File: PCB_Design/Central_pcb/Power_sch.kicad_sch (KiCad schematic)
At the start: 1 part

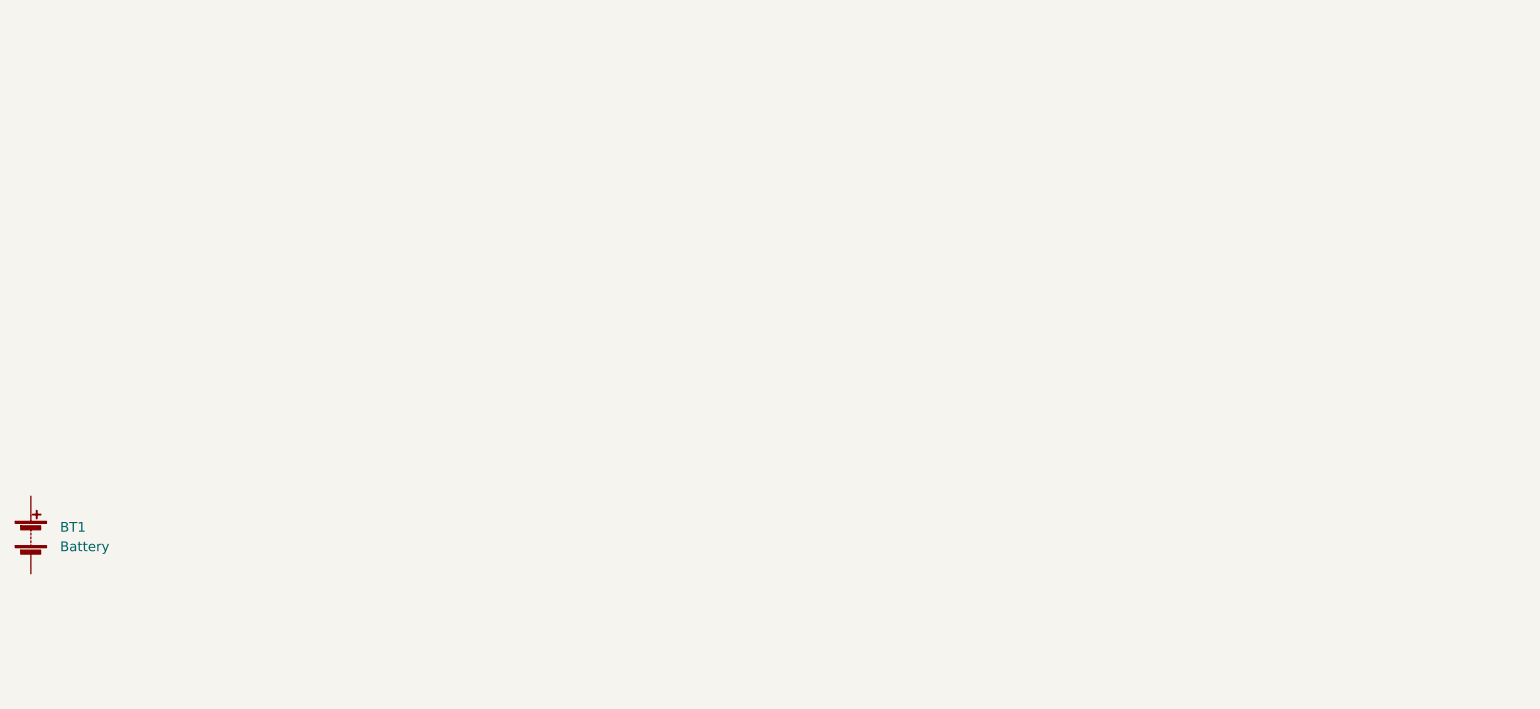
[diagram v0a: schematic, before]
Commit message: Power part added
Power part is finished with power footprints
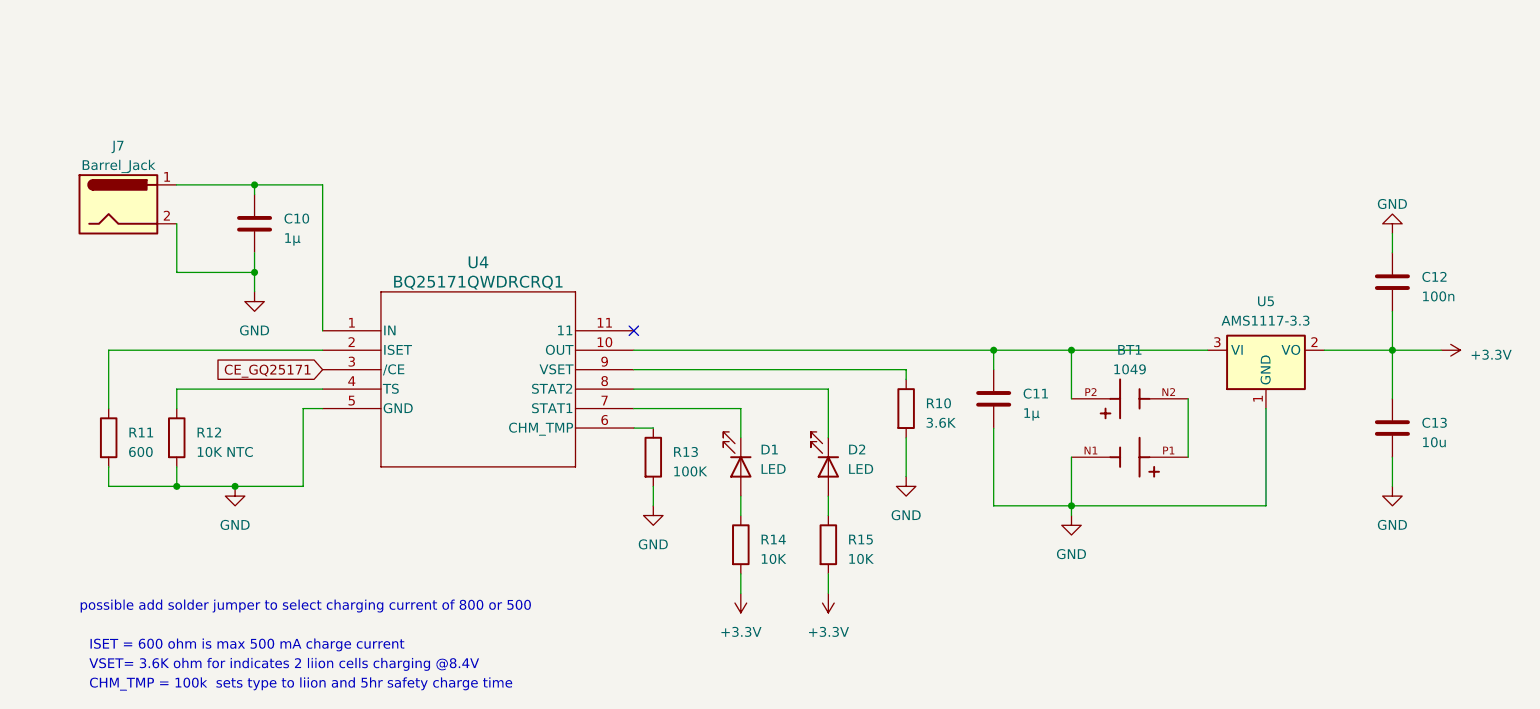
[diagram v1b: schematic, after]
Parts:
- removed BT1: Battery, symbol Device:Battery
- added BT1: 1049, Central:BAT_1049, symbol 1049P:1049
- added C10, C11: 1µ, Capacitor_SMD:C_0805_2012Metric_Pad1.18x1.45mm_HandSolder, symbol Device:C
- added C12: 100n, Capacitor_SMD:C_0805_2012Metric_Pad1.18x1.45mm_HandSolder, symbol Device:C
- added C13: 10u, Capacitor_SMD:C_0805_2012Metric_Pad1.18x1.45mm_HandSolder, symbol Device:C
- added D1, D2: LED, LED_SMD:LED_0805_2012Metric_Pad1.15x1.40mm_HandSolder, symbol Device:LED
- added J7: Barrel_Jack, Connector_BarrelJack:BarrelJack_GCT_DCJ200-10-A_Horizontal, symbol Connector:Barrel_Jack
- added R10: 3.6K, Resistor_SMD:R_0805_2012Metric_Pad1.20x1.40mm_HandSolder, symbol Device:R
- added R11: 600, Resistor_SMD:R_0805_2012Metric_Pad1.20x1.40mm_HandSolder, symbol Device:R
- added R12: 10K NTC, symbol Device:R
- added R13: 100K, Resistor_SMD:R_0805_2012Metric_Pad1.20x1.40mm_HandSolder, symbol Device:R
- added R14, R15: 10K, Resistor_SMD:R_0805_2012Metric_Pad1.20x1.40mm_HandSolder, symbol Device:R
- added U4: BQ25171QWDRCRQ1, Central:VSON10_BQ25171_3X3_TEX, symbol BQ25171:BQ25171QWDRCRQ1
- added U5: AMS1117-3.3, Package_TO_SOT_SMD:SOT-223-3_TabPin2, symbol Regulator_Linear:AMS1117-3.3
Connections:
- new net: D2.1 (K), U4.8 (STAT2)
- new net: D2.2 (A), R15.1
- new net: C10.1, J7.1, U4.1 (IN)
- new net: R11.1, U4.2 (ISET)
- new net: BT1.N2, BT1.P1
- new net: BT1.P2, C11.1, U4.10 (OUT), U5.3 (VI)
- new net: R13.1, U4.6 (CHM_TMP)
- new net: D1.1 (K), U4.7 (STAT1)
- new net: D1.2 (A), R14.1
- new net: R12.1, U4.4 (TS)
- new net: R10.1, U4.9 (VSET)
- new net +3.3V: C12.2, C13.1, R14.2, R15.2, U5.2 (VO)
- new net CE_GQ25171: U4.3 (/CE)
- new net GND: BT1.N1, C10.2, C11.2, C12.1, C13.2, J7.2, R10.2, R11.2, R12.2, R13.2, U4.5 (GND), U5.1 (GND)
- no-connect marks 0 -> 1
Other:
- note added: "CHM_TMP = 100k sets type to liion and 5hr safety charge time"
- note added: "ISET = 600 ohm is max 500 mA charge current"
- note added: "VSET= 3.6K ohm for indicates 2 liion cells charging @8.4V"
- note added: "possible add solder jumper to select charging current of 800 or 500"

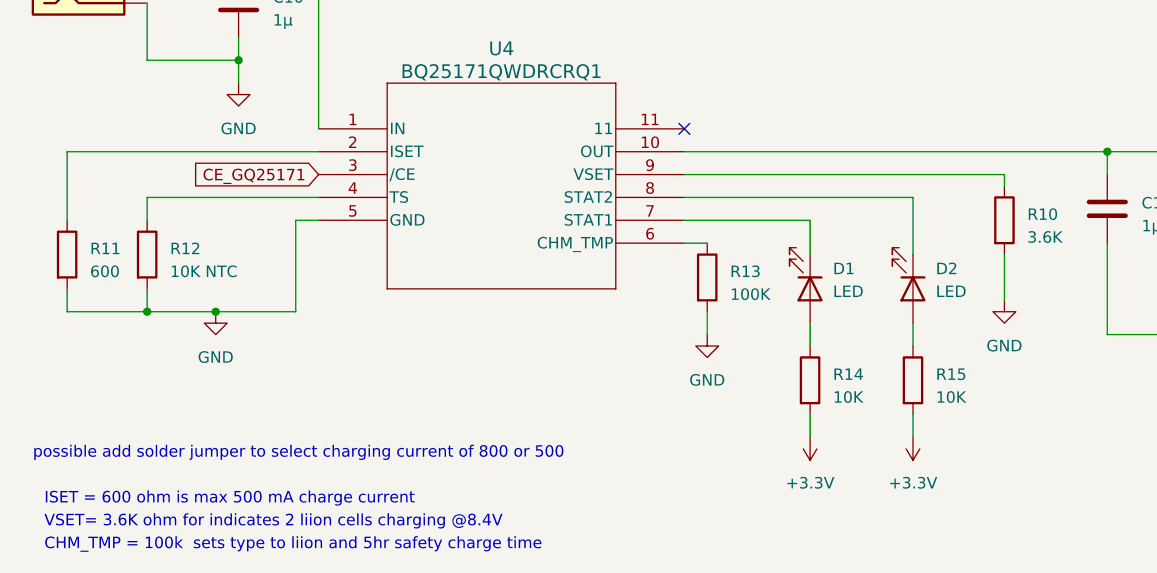
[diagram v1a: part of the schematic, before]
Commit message: Scematic update
update scematic and added some footrpints
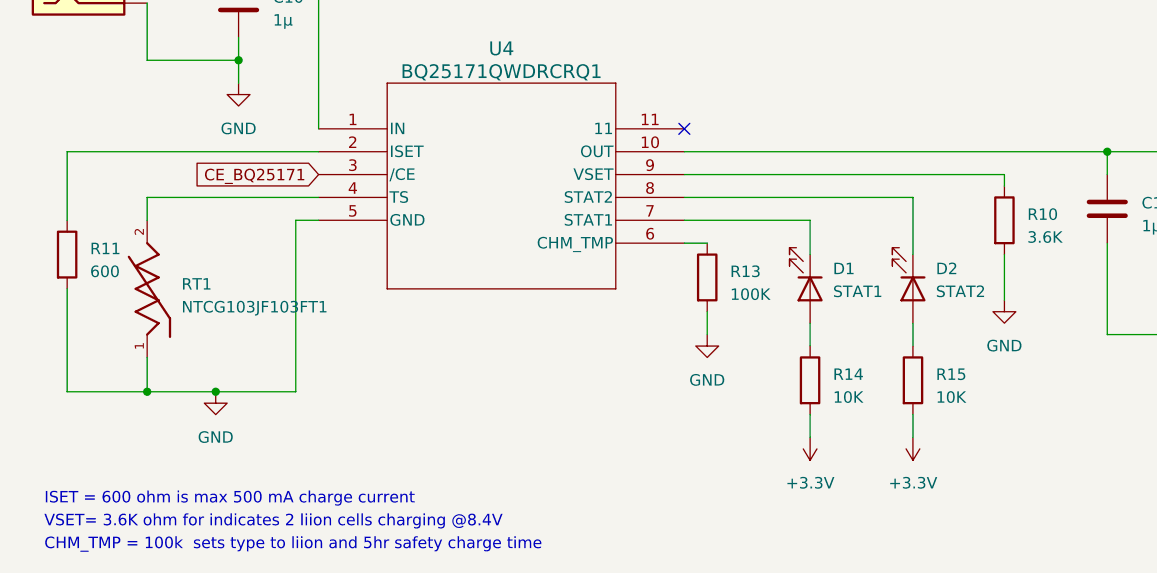
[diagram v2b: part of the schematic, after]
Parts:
- removed R12: 10K NTC, symbol Device:R
- added RT1: NTCG103JF103FT1, Central:THERM_NTCG103JF103FT1, symbol 10K NTC:NTCG103JF103FT1
- D1: value LED -> STAT1
- D2: value LED -> STAT2
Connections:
- net GND: now also RT1.1
- net at U4.4 (TS): now also RT1.2
- net CE_GQ25171 renamed CE_BQ25171
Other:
- note removed: "possible add solder jumper to select charging current of 800 or 500"
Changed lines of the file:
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@@
   (junction (at 210.82 73.66) (diameter 0) (color 0 0 0 0)
   )
+  (junction (at 93.98 100.33) (diameter 0) (color 0 0 0 0)
+  )
   (junction (at 210.82 93.98) (diameter 0) (color 0 0 0 0)
   )
@@
   (junction (at 200.66 73.66) (diameter 0) (color 0 0 0 0)
   )
-  (junction (at 101.6 91.44) (diameter 0) (color 0 0 0 0)
+  (junction (at 101.6 100.33) (diameter 0) (color 0 0 0 0)
   )
   (junction (at 252.73 73.66) (diameter 0) (color 0 0 0 0)
-  )
-  (junction (at 93.98 91.44) (diameter 0) (color 0 0 0 0)
   )
   (junction (at 104.14 63.5) (diameter 0) (color 0 0 0 0)
@@
     (stroke (width 0) (type default))
   )
-  (wire (pts (xy 101.6 91.44) (xy 110.49 91.44))
+  (wire (pts (xy 101.6 100.33) (xy 110.49 100.33))
     (stroke (width 0) (type default))
   )
@@
     (stroke (width 0) (type default))
   )
-  (wire (pts (xy 93.98 88.9) (xy 93.98 91.44))
-    (stroke (width 0) (type default))
-  )
   (wire (pts (xy 252.73 58.42) (xy 252.73 60.96))
     (stroke (width 0) (type default))
@@
     (stroke (width 0) (type default))
   )
+  (wire (pts (xy 93.98 100.33) (xy 101.6 100.33))
+    (stroke (width 0) (type default))
+  )
+  (wire (pts (xy 93.98 96.52) (xy 93.98 100.33))
+    (stroke (width 0) (type default))
+  )
   (wire (pts (xy 200.66 73.66) (xy 210.82 73.66))
     (stroke (width 0) (type default))
@@
     (stroke (width 0) (type default))
   )
-  (wire (pts (xy 93.98 91.44) (xy 101.6 91.44))
+  (wire (pts (xy 85.09 100.33) (xy 93.98 100.33))
     (stroke (width 0) (type default))
   )
@@
     (stroke (width 0) (type default))
   )
-  (wire (pts (xy 85.09 88.9) (xy 85.09 91.44))
+  (wire (pts (xy 85.09 88.9) (xy 85.09 100.33))
     (stroke (width 0) (type default))
   )
@@
     (stroke (width 0) (type default))
   )
-  (wire (pts (xy 110.49 81.28) (xy 110.49 91.44))
+  (wire (pts (xy 110.49 81.28) (xy 110.49 100.33))
     (stroke (width 0) (type default))
   )
@@
     (stroke (width 0) (type default))
   )
-  (wire (pts (xy 85.09 91.44) (xy 93.98 91.44))
-    (stroke (width 0) (type default))
-  )
   (wire (pts (xy 189.23 76.2) (xy 189.23 77.47))
     (stroke (width 0) (type default))
@@
   )
   (text "ISET = 600 ohm is max 500 mA charge current\n" (at 82.55 113.03 0)
-    (effects (font (size 1.27 1.27)) (justify left bottom))
-  )
-  (text "possible add solder jumper to select charging current of 800 or 500"
-    (at 81.28 107.95 0)
     (effects (font (size 1.27 1.27)) (justify left bottom))
   )
@@
     (effects (font (size 1.27 1.27)) (justify left bottom))
   )
-  (global_label "CE_GQ25171" (shape input) (at 113.03 76.2 180) (fields_autoplaced)
+  (global_label "CE_BQ25171" (shape input) (at 113.03 76.2 180) (fields_autoplaced)
     (effects (font (size 1.27 1.27)) (justify right))
     (property "Intersheetrefs" "${INTERSHEET_REFS}" (at 98.0896 76.2 0)
@@
       (effects (font (size 1.27 1.27)) (justify left))
     )
-    (property "Value" "LED" (at 181.61 89.2175 90)
+    (property "Value" "STAT2" (at 181.61 89.2175 90)
       (effects (font (size 1.27 1.27)) (justify left))
     )
@@
     )
   )
+  (symbol (lib_id "10K NTC:NTCG103JF103FT1") (at 93.98 88.9 90) (unit 1)
+    (in_bom yes) (on_board yes) (dnp no) (fields_autoplaced)
+    (property "Reference" "RT1" (at 97.79 88.392 90)
+      (effects (font (size 1.27 1.27)) (justify right))
+    )
+    (property "Value" "NTCG103JF103FT1" (at 97.79 90.932 90)
+      (effects (font (size 1.27 1.27)) (justify right))
+    )
+    (property "Footprint" "Central:THERM_NTCG103JF103FT1" (at 93.98 88.9 0)
+      (effects (font (size 1.27 1.27)) (justify bottom) hide)
+    )
+    (property "Datasheet" "" (at 93.98 88.9 0)
+      (effects (font (size 1.27 1.27)) hide)
+    )
+    (property "MF" "TDK" (at 93.98 88.9 0)
+      (effects (font (size 1.27 1.27)) (justify bottom) hide)
+    )
+    (property "MAXIMUM_PACKAGE_HEIGHT" "0.55 mm" (at 93.98 88.9 0)
+      (effects (font (size 1.27 1.27)) (justify bottom) hide)
+    )
+    (property "Package" "0402 TDK" (at 93.98 88.9 0)
+      (effects (font (size 1.27 1.27)) (justify bottom) hide)
+    )
+    (property "Price" "None" (at 93.98 88.9 0)
+      (effects (font (size 1.27 1.27)) (justify bottom) hide)
+    )
+    (property "Check_prices" "https://www.snapeda.com/parts/NTCG103JF103FT1/TDK/view-part/?ref=eda" (at 93.98 88.9 0)
+      (effects (font (size 1.27 1.27)) (justify bottom) hide)
+    )
+    (property "STANDARD" "Manufacturer Recommendations" (at 93.98 88.9 0)
+      (effects (font (size 1.27 1.27)) (justify bottom) hide)
+    )
+    (property "PARTREV" "8/12/2022" (at 93.98 88.9 0)
+      (effects (font (size 1.27 1.27)) (justify bottom) hide)
+    )
+    (property "SnapEDA_Link" "https://www.snapeda.com/parts/NTCG103JF103FT1/TDK/view-part/?ref=snap" (at 93.98 88.9 0)
+      (effects (font (size 1.27 1.27)) (justify bottom) hide)
+    )
+    (property "MP" "NTCG103JF103FT1" (at 93.98 88.9 0)
+      (effects (font (size 1.27 1.27)) (justify bottom) hide)
+    )
+    (property "Purchase-URL" "https://www.snapeda.com/api/url_track_click_mouser/?unipart_id=696931&manufacturer=TDK&part_name=NTCG103JF103FT1&search_term=None" (at 93.98 88.9 0)
+      (effects (font (size 1.27 1.27)) (justify bottom) hide)
+    )
+    (property "Description" "\nNTC Thermistor 10k 0402 (1005 Metric)\n" (at 93.98 88.9 0)
+      (effects (font (size 1.27 1.27)) (justify bottom) hide)
+    )
+    (property "Availability" "In Stock" (at 93.98 88.9 0)
+      (effects (font (size 1.27 1.27)) (justify bottom) hide)
+    )
+    (property "MANUFACTURER" "TDK" (at 93.98 88.9 0)
+      (effects (font (size 1.27 1.27)) (justify bottom) hide)
+    )
+    (pin "1")
+    (pin "2")
+    (instances
+      (project "Central_pcb"
+        (path "/4d244925-fc91-48ed-8daa-e4f0d6afeb7f/3414a10a-973a-4a85-bec5-f896220b0f20"
+          (reference "RT1") (unit 1)
+        )
+      )
+    )
+  )
   (symbol (lib_id "Device:C") (at 252.73 64.77 0) (unit 1)
     (in_bom yes) (on_board yes) (dnp no) (fields_autoplaced)
@@
       (effects (font (size 1.27 1.27)) (justify left))
     )
-    (property "Value" "LED" (at 170.18 89.2175 90)
+    (property "Value" "STAT1" (at 170.18 89.2175 90)
       (effects (font (size 1.27 1.27)) (justify left))
     )
@@
     )
   )
-  (symbol (lib_id "power:GND") (at 101.6 91.44 0) (unit 1)
-    (in_bom yes) (on_board yes) (dnp no) (fields_autoplaced)
-    (property "Reference" "#PWR016" (at 101.6 97.79 0)
-      (effects (font (size 1.27 1.27)) hide)
-    )
-    (property "Value" "GND" (at 101.6 96.52 0)
-      (effects (font (size 1.27 1.27)))
-    )
-    (property "Footprint" "" (at 101.6 91.44 0)
-      (effects (font (size 1.27 1.27)) hide)
-    )
-    (property "Datasheet" "" (at 101.6 91.44 0)
+  (symbol (lib_id "power:GND") (at 101.6 100.33 0) (unit 1)
+    (in_bom yes) (on_board yes) (dnp no) (fields_autoplaced)
+    (property "Reference" "#PWR016" (at 101.6 106.68 0)
+      (effects (font (size 1.27 1.27)) hide)
+    )
+    (property "Value" "GND" (at 101.6 105.41 0)
+      (effects (font (size 1.27 1.27)))
+    )
+    (property "Footprint" "" (at 101.6 100.33 0)
+      (effects (font (size 1.27 1.27)) hide)
+    )
+    (property "Datasheet" "" (at 101.6 100.33 0)
       (effects (font (size 1.27 1.27)) hide)
     )
@@
         )
       )
-    )
-  )
-  (symbol (lib_id "Device:R") (at 93.98 85.09 0) (unit 1)
-    (in_bom yes) (on_board yes) (dnp no) (fields_autoplaced)
-    (property "Reference" "R12" (at 96.52 84.455 0)
-      (effects (font (size 1.27 1.27)) (justify left))
-    )
-    (property "Value" "10K NTC" (at 96.52 86.995 0)
-      (effects (font (size 1.27 1.27)) (justify left))
-    )
-    (property "Footprint" "" (at 92.202 85.09 90)
-      (effects (font (size 1.27 1.27)) hide)
-    )
-    (property "Datasheet" "~" (at 93.98 85.09 0)
-      (effects (font (size 1.27 1.27)) hide)
-    )
-    (pin "1")
-    (pin "2")
-    (instances
-      (project "Central_pcb"
-        (path "/4d244925-fc91-48ed-8daa-e4f0d6afeb7f/3414a10a-973a-4a85-bec5-f896220b0f20"
-          (reference "R12") (unit 1)
-        )
-      )

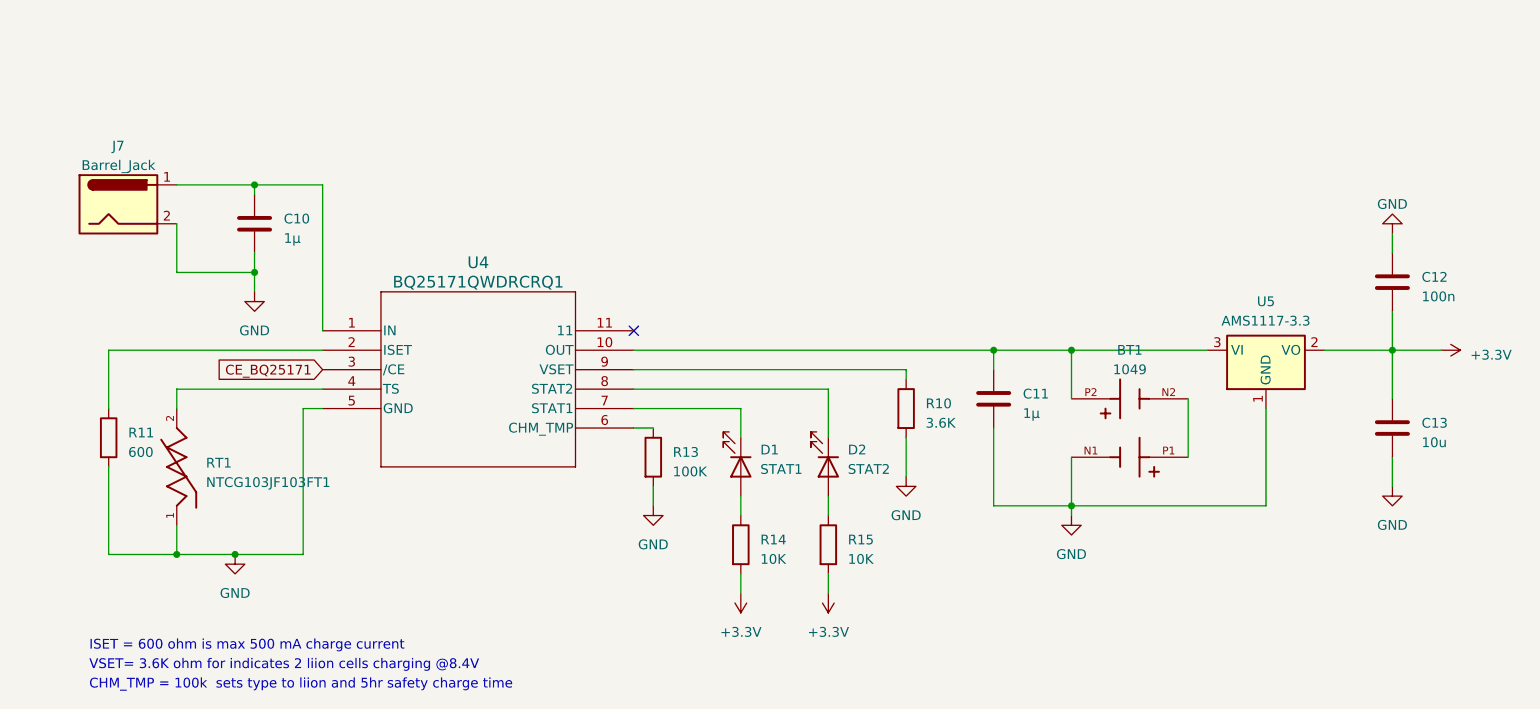
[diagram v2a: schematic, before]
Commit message: Initial PCB design
Rough sketch of what the layout could be
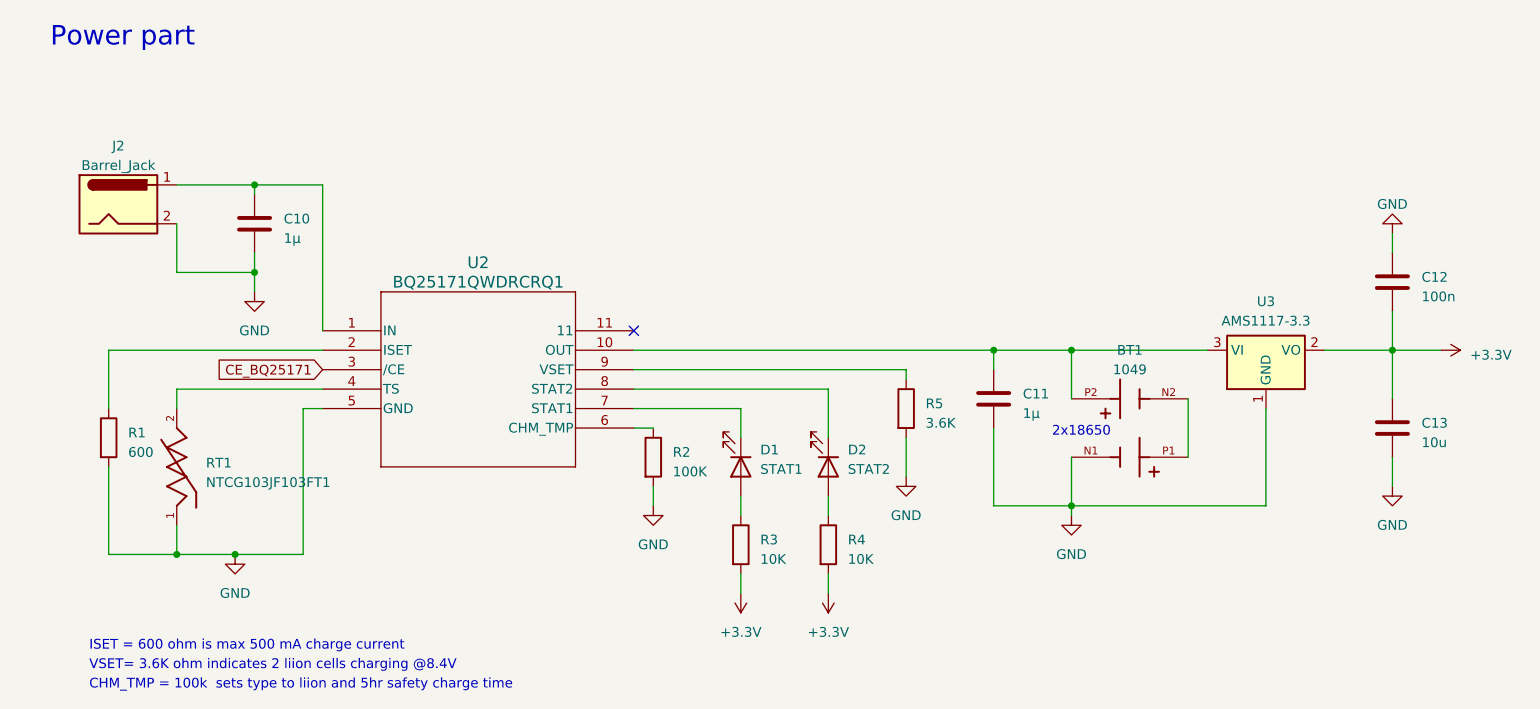
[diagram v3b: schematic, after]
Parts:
- renumbered J7 to J2, R11 to R1, R13 to R2, R14 to R3, R15 to R4, R10 to R5, U4 to U2, U5 to U3
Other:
- note added: "2x18650"
- note added: "Power part"
- note added: "VSET= 3.6K ohm indicates 2 liion cells charging @8.4V"
- note removed: "VSET= 3.6K ohm for indicates 2 liion cells charging @8.4V"
